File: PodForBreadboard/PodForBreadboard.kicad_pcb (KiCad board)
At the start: 2 copper layers, 14.2 x 15.2 mm, 3 parts, among them J1 Conn_02x02_Odd_Even, J2 Conn_01x04

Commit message: 細かな調整
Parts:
- moved J1 2.54 mm to (106.7, 59.7)
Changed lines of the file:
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@@
   )
   (footprint "Connector_PinHeader_2.54mm:PinHeader_2x02_P2.54mm_Vertical" (layer "B.Cu")
-    (at 106.675 57.145 -90)
+    (at 106.675 59.69 -90)
     (descr "Through hole straight pin header, 2x02, 2.54mm pitch, double rows")
     (tags "Through hole pin header THT 2x02 2.54mm double row")
@@
     )
   )
-  (gr_line (start 110.49 57.15) (end 113.538 57.15) (layer "F.SilkS") (width 0.4))
-  (gr_line (start 101.6 57.15) (end 105.41 57.15) (layer "F.SilkS") (width 0.4))
-  (gr_rect (start 105.537 68.707) (end 110.363 70.993) (layer "F.SilkS") (width 0.2) (fill none))
+  (gr_line (start 101.346 62.992) (end 114.554 62.992) (layer "F.SilkS") (width 0.6))
+  (gr_line (start 101.346 58.928) (end 114.554 58.928) (layer "F.SilkS") (width 0.6))
+  (gr_rect (start 105.537 68.834) (end 110.363 70.866) (layer "F.SilkS") (width 0.3) (fill none))
   (gr_rect (start 100.838 55.88) (end 115.062 71.12) (layer "Edge.Cuts") (width 0.1) (fill none))
   (gr_text "JLCJLCJLCJLC" (at 108.204 65.024) (layer "B.SilkS")
@@
     (effects (font (size 1 1) (thickness 0.15)))
   )
-  (gr_text "V" (at 114.3 57.15) (layer "F.SilkS")
-    (effects (font (size 1 1) (thickness 0.15)))
+  (gr_text "V" (at 114.3 57.912) (layer "F.SilkS")
+    (effects (font (size 1.2 1.2) (thickness 0.15)))
   )
   (gr_text "G" (at 102.616 69.85) (layer "F.SilkS")
     (effects (font (size 1 1) (thickness 0.15)))
   )
+  (gr_text "G" (at 114.3 64.262) (layer "F.SilkS")
+    (effects (font (size 1.2 1.2) (thickness 0.15)))
+  )
   (dimension (type aligned) (layer "F.Fab")
-    (pts (xy 112.024027 59.69) (xy 112.024027 69.85))
+    (pts (xy 112.024027 62.23) (xy 112.024027 69.85))
     (height -6.339973)
-    (gr_text "10.1600 mm" (at 117.214 64.77 90) (layer "F.Fab")
+    (gr_text "7.6200 mm" (at 117.214 66.04 90) (layer "F.Fab")
       (effects (font (size 1 1) (thickness 0.15)))
     )

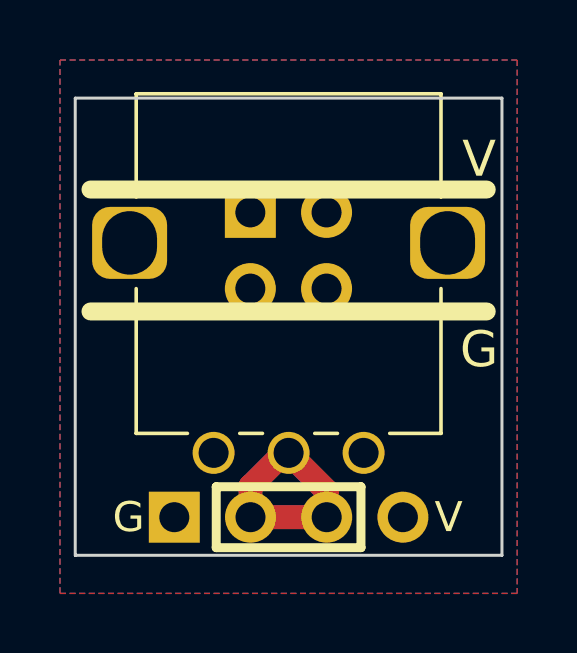
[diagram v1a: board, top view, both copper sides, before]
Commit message: Pod for BB
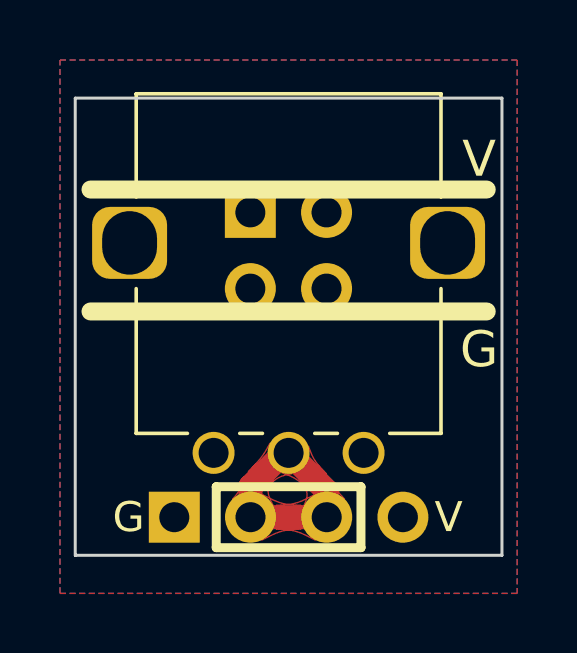
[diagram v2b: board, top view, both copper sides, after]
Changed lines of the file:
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@@
   (segment (start 107.95 67.706) (end 107.794 67.706) (width 0.8) (layer "F.Cu") (net 2))
   (segment (start 109.22 68.976) (end 107.95 67.706) (width 0.8) (layer "F.Cu") (net 2))
+  (zone (net 2) (net_name "/2") (layer "F.Cu") (hatch edge 0.508)
+    (priority 16962)
+    (connect_pads yes (clearance 0))
+    (min_thickness 0.0254) (filled_areas_thickness no)
+    (fill yes (thermal_gap 0.508) (thermal_bridge_width 0.508))
+    (polygon
+      (pts
+        (xy 109.21572 68.406035)
+        (xy 109.107284 68.295567)
+        (xy 109.015684 68.197329)
+        (xy 108.938607 68.108193)
+        (xy 108.873737 68.02503)
+        (xy 108.818759 67.944711)
+        (xy 108.771358 67.864108)
+        (xy 108.72922 67.780092)
+        (xy 108.690029 67.689534)
+        (xy 108.651471 67.589305)
+        (xy 108.611231 67.476278)
+        (xy 107.702513 67.458513)
+        (xy 107.720278 68.367231)
+        (xy 107.833305 68.407471)
+        (xy 107.933534 68.446029)
+        (xy 108.024092 68.48522)
+        (xy 108.108108 68.527358)
+        (xy 108.188711 68.574759)
+        (xy 108.26903 68.629737)
+        (xy 108.352193 68.694607)
+        (xy 108.441329 68.771684)
+        (xy 108.539567 68.863284)
+        (xy 108.650035 68.97172)
+      )
+    )
+  )
+  (zone (net 2) (net_name "/2") (layer "F.Cu") (hatch edge 0.508)
+    (priority 16962)
+    (connect_pads yes (clearance 0))
+    (min_thickness 0.0254) (filled_areas_thickness no)
+    (fill yes (thermal_gap 0.508) (thermal_bridge_width 0.508))
+    (polygon
+      (pts
+        (xy 107.164675 68.90101)
+        (xy 107.268946 68.799337)
+        (xy 107.362847 68.713872)
+        (xy 107.449155 68.642791)
+        (xy 107.530647 68.584273)
+        (xy 107.610102 68.536495)
+        (xy 107.690297 68.497635)
+        (xy 107.77401 68.46587)
+        (xy 107.86402 68.439377)
+        (xy 107.963103 68.416335)
+        (xy 108.074039 68.394922)
+        (xy 108.232981 67.500035)
+        (xy 107.332566 67.376191)
+        (xy 107.270557 67.490732)
+        (xy 107.213512 67.591736)
+        (xy 107.158624 67.682728)
+        (xy 107.103085 67.76723)
+        (xy 107.044089 67.848768)
+        (xy 106.978828 67.930866)
+        (xy 106.904494 68.017046)
+        (xy 106.818282 68.110833)
+        (xy 106.717382 68.215751)
+        (xy 106.59899 68.335325)
+      )
+    )
+  )
+  (zone (net 2) (net_name "/2") (layer "F.Cu") (hatch edge 0.508)
+    (priority 16962)
+    (connect_pads yes (clearance 0))
+    (min_thickness 0.0254) (filled_areas_thickness no)
+    (fill yes (thermal_gap 0.508) (thermal_bridge_width 0.508))
+    (polygon
+      (pts
+        (xy 108.37 69.45)
+        (xy 108.180206 69.446314)
+        (xy 108.017887 69.435273)
+        (xy 107.877558 69.416901)
+        (xy 107.753738 69.39122)
+        (xy 107.640945 69.358256)
+        (xy 107.533696 69.318031)
+        (xy 107.42651 69.270569)
+        (xy 107.313904 69.215894)
+        (xy 107.190397 69.15403)
+        (xy 107.050506 69.085)
+        (xy 106.255 69.85)
+        (xy 107.050506 70.615)
+        (xy 107.190397 70.545969)
+        (xy 107.313904 70.484105)
+        (xy 107.42651 70.42943)
+        (xy 107.533696 70.381968)
+        (xy 107.640945 70.341743)
+        (xy 107.753738 70.308779)
+        (xy 107.877558 70.283098)
+        (xy 108.017887 70.264726)
+        (xy 108.180206 70.253685)
+        (xy 108.37 70.25)
+      )
+    )
+  )
   (zone (net 3) (net_name "VDD") (layer "F.Cu") (hatch edge 0.508)
     (connect_pads (clearance 0.508))
@@
       )
     )
+  )
+  (zone (net 2) (net_name "/2") (layer "F.Cu") (hatch edge 0.508)
+    (priority 16962)
+    (connect_pads yes (clearance 0))
+    (min_thickness 0.0254) (filled_areas_thickness no)
+    (fill yes (thermal_gap 0.508) (thermal_bridge_width 0.508))
+    (polygon
+      (pts
+        (xy 106.870918 68.063396)
+        (xy 106.737291 68.208043)
+        (xy 106.634239 68.341009)
+        (xy 106.554831 68.464501)
+        (xy 106.492139 68.580723)
+        (xy 106.439233 68.691883)
+        (xy 106.389183 68.800187)
+        (xy 106.33506 68.90784)
+        (xy 106.269935 69.017049)
+        (xy 106.186878 69.13002)
+        (xy 106.07896 69.24896)
+        (xy 106.68 70.275)
+        (xy 107.445 69.479494)
+        (xy 107.400113 69.388369)
+        (xy 107.35753 69.300716)
+        (xy 107.320057 69.21574)
+        (xy 107.290501 69.132645)
+        (xy 107.271668 69.050637)
+        (xy 107.266367 68.968921)
+        (xy 107.277402 68.886702)
+        (xy 107.307583 68.803186)
+        (xy 107.359714 68.717577)
+        (xy 107.436604 68.629082)
+      )
+    )
+  )
+  (zone (net 2) (net_name "/2") (layer "F.Cu") (hatch edge 0.508)
+    (priority 16962)
+    (connect_pads yes (clearance 0))
+    (min_thickness 0.0254) (filled_areas_thickness no)
+    (fill yes (thermal_gap 0.508) (thermal_bridge_width 0.508))
+    (polygon
+      (pts
+        (xy 108.353088 68.674773)
+        (xy 108.429501 68.758999)
+        (xy 108.487577 68.840166)
+        (xy 108.528674 68.919107)
+        (xy 108.554148 68.996657)
+        (xy 108.56536 69.073651)
+        (xy 108.563666 69.150924)
+        (xy 108.550425 69.229309)
+        (xy 108.526995 69.309643)
+        (xy 108.494734 69.39276)
+        (xy 108.455 69.479494)
+        (xy 109.22 70.275)
+        (xy 109.82104 69.24896)
+        (xy 109.708348 69.129615)
+        (xy 109.616459 69.019668)
+        (xy 109.539442 68.916039)
+        (xy 109.471369 68.815653)
+        (xy 109.406313 68.715431)
+        (xy 109.338344 68.612296)
+        (xy 109.261534 68.503172)
+        (xy 109.169954 68.38498)
+        (xy 109.057677 68.254645)
+        (xy 108.918773 68.109088)
+      )
+    )
+  )
+  (zone (net 2) (net_name "/2") (layer "F.Cu") (hatch edge 0.508)
+    (priority 16962)
+    (connect_pads yes (clearance 0))
+    (min_thickness 0.0254) (filled_areas_thickness no)
+    (fill yes (thermal_gap 0.508) (thermal_bridge_width 0.508))
+    (polygon
+      (pts
+        (xy 107.53 70.25)
+        (xy 107.719793 70.253685)
+        (xy 107.882112 70.264726)
+        (xy 108.022441 70.283098)
+        (xy 108.146261 70.308779)
+        (xy 108.259054 70.341743)
+        (xy 108.366303 70.381968)
+        (xy 108.473489 70.42943)
+        (xy 108.586095 70.484105)
+        (xy 108.709602 70.545969)
+        (xy 108.849494 70.615)
+        (xy 109.645 69.85)
+        (xy 108.849494 69.085)
+        (xy 108.709602 69.15403)
+        (xy 108.586095 69.215894)
+        (xy 108.473489 69.270569)
+        (xy 108.366303 69.318031)
+        (xy 108.259054 69.358256)
+        (xy 108.146261 69.39122)
+        (xy 108.022441 69.416901)
+        (xy 107.882112 69.435273)
+        (xy 107.719793 69.446314)
+        (xy 107.53 69.45)
+      )
+    )
